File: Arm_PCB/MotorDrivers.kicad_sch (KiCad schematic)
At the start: 52 parts, among them J19 Conn_02x03_Counter_Clockwise, J20 Conn_02x03_Counter_Clockwise, U1 TB6560_Board, U10 TB6560_Board, U11 INA219AxDCN, U12 TB6560_Board, U13 INA219AxDCN, U14 TB6560_Board, U15 INA219AxDCN, U16 TB6560_Board, U2 INA219AxDCN, U3 INA219AxDCN, U4 INA219AxDCN, U5 TB6560_Board, U6 INA219AxDCN, U7 TB6560_Board, U8 INA219AxDCN, U9 INA219AxDCN

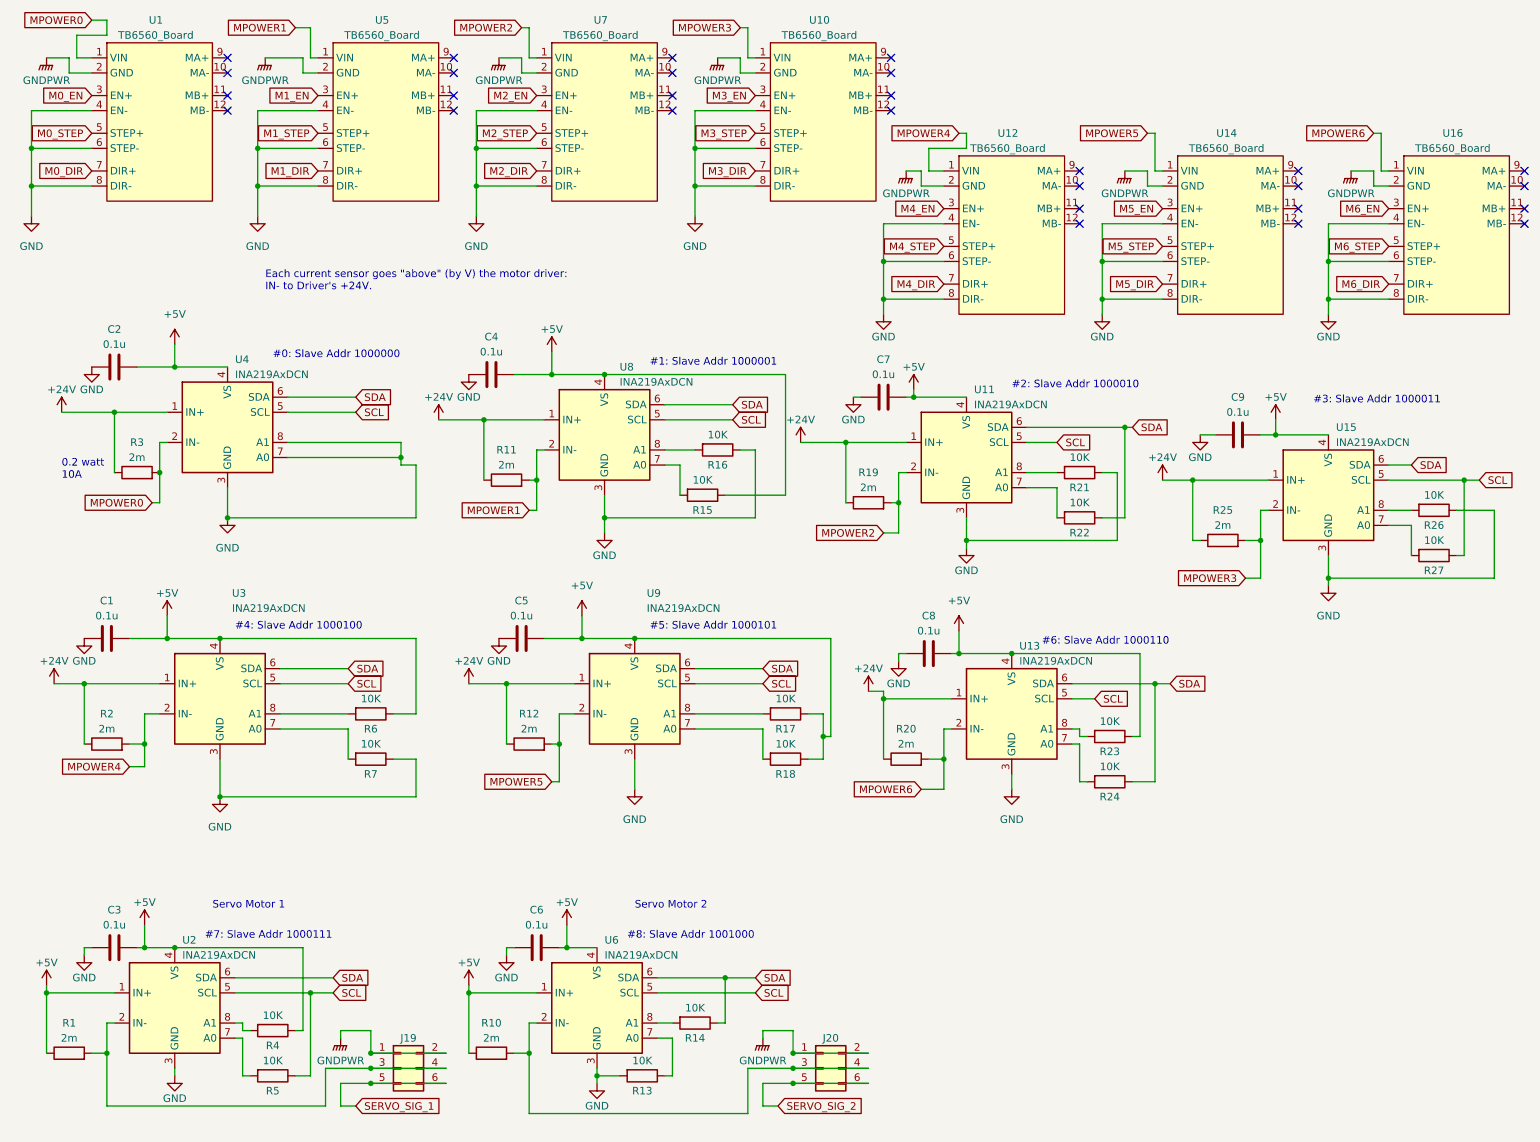
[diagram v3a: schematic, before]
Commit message: Remove resistors for setting I2C addrs
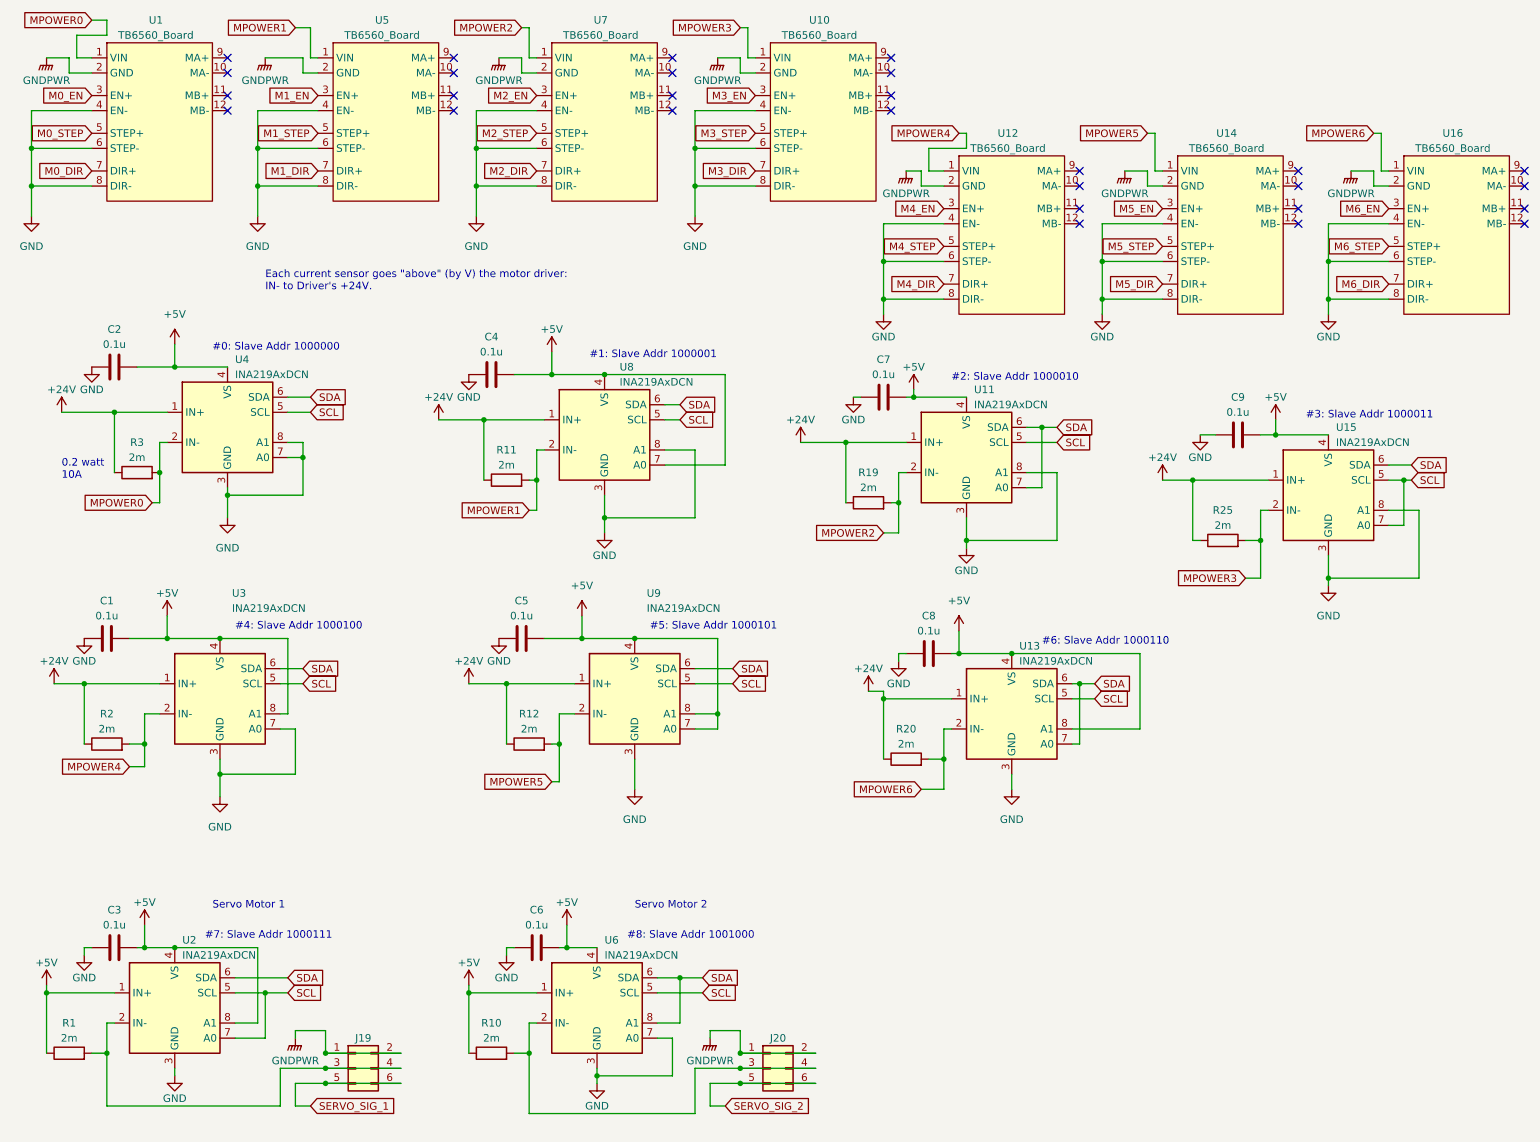
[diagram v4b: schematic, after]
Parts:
- removed R13, R14, R15, R16, R17, R18, R21, R22, R23, R24, R26, R27, R4, R5, R6, R7: 10K, Resistor_SMD:R_1206_3216Metric_Pad1.30x1.75mm_HandSolder, symbol Device:R
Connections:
- net +5V: now also U13.8 (A1), U2.8 (A1), U3.8 (A1), U8.7 (A0), U9.7 (A0), U9.8 (A1)
- net GND: now also U11.8 (A1), U15.8 (A1), U3.7 (A0), U6.7 (A0), U8.8 (A1)
- net SCL: now also U15.7 (A0), U2.7 (A0)
- net SDA: now also U11.7 (A0), U13.7 (A0), U6.8 (A1)
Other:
- moved on the sheet: J19, J20

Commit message: Route more
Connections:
- net S_POWER_2: now reaches J20.3 (Pin_3), J20.4 (Pin_4), R10.2, U6.2 (IN-)
- net S_POWER_1: now reaches J19.3 (Pin_3), J19.4 (Pin_4), R1.2, U2.2 (IN-)
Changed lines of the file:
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@@
   (junction (at 133.35 189.23) (diameter 0) (color 0 0 0 0)
+  )
+  (junction (at 113.03 199.39) (diameter 0) (color 0 0 0 0)
+  )
+  (junction (at 41.91 198.12) (diameter 0) (color 0 0 0 0)
   )
   (junction (at 171.45 102.87) (diameter 0) (color 0 0 0 0)
@@
     (stroke (width 0) (type default))
   )
+  (wire (pts (xy 113.03 201.93) (xy 113.03 199.39))
+    (stroke (width 0) (type default))
+  )
   (wire (pts (xy 16.51 177.8) (xy 16.51 179.07))
     (stroke (width 0) (type default))
@@
     (stroke (width 0) (type default))
   )
-  (wire (pts (xy 97.79 199.39) (xy 125.73 199.39))
+  (wire (pts (xy 97.79 199.39) (xy 113.03 199.39))
     (stroke (width 0) (type default))
   )
@@
     (stroke (width 0) (type default))
   )
+  (wire (pts (xy 41.91 200.66) (xy 41.91 198.12))
+    (stroke (width 0) (type default))
+  )
   (wire (pts (xy 63.5 194.31) (xy 58.42 194.31))
     (stroke (width 0) (type default))
@@
     (stroke (width 0) (type default))
   )
-  (wire (pts (xy 26.67 198.12) (xy 55.88 198.12))
+  (wire (pts (xy 26.67 198.12) (xy 41.91 198.12))
     (stroke (width 0) (type default))
   )
@@
     (stroke (width 0) (type default))
   )
+  (wire (pts (xy 41.91 198.12) (xy 55.88 198.12))
+    (stroke (width 0) (type default))
+  )
   (wire (pts (xy 247.65 97.79) (xy 247.65 109.22))
     (stroke (width 0) (type default))
@@
   )
   (wire (pts (xy 129.54 132.08) (xy 129.54 119.38))
+    (stroke (width 0) (type default))
+  )
+  (wire (pts (xy 113.03 199.39) (xy 125.73 199.39))
     (stroke (width 0) (type default))
   )
@@
     (effects (font (size 1.27 1.27)) (justify left bottom))
   )
+  (label "S_POWER_1" (at 41.91 200.66 0) (fields_autoplaced)
+    (effects (font (size 1.27 1.27)) (justify left bottom))
+  )
+  (label "S_POWER_2" (at 113.03 201.93 0) (fields_autoplaced)
+    (effects (font (size 1.27 1.27)) (justify left bottom))
+  )
